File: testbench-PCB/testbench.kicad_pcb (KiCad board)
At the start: 2 copper layers, 185.4 x 134.6 mm, 68 parts, among them J1 USB_C_Receptacle_USB2.0, J2 AVR-ISP, J3 AVR-JTAG, SW1 SW_Push, U1 ATmega2561-16A, U10 CH340C, U2 Thermistor_module, U3 Rotary_encoder_switch_module, U4 RTC_EEPROM_module, U6 Relay_module, U7 Matrix_keyboard, U8 LCD_display, U9 USBLC6-2SC6, Y1 X322516MLB4SI

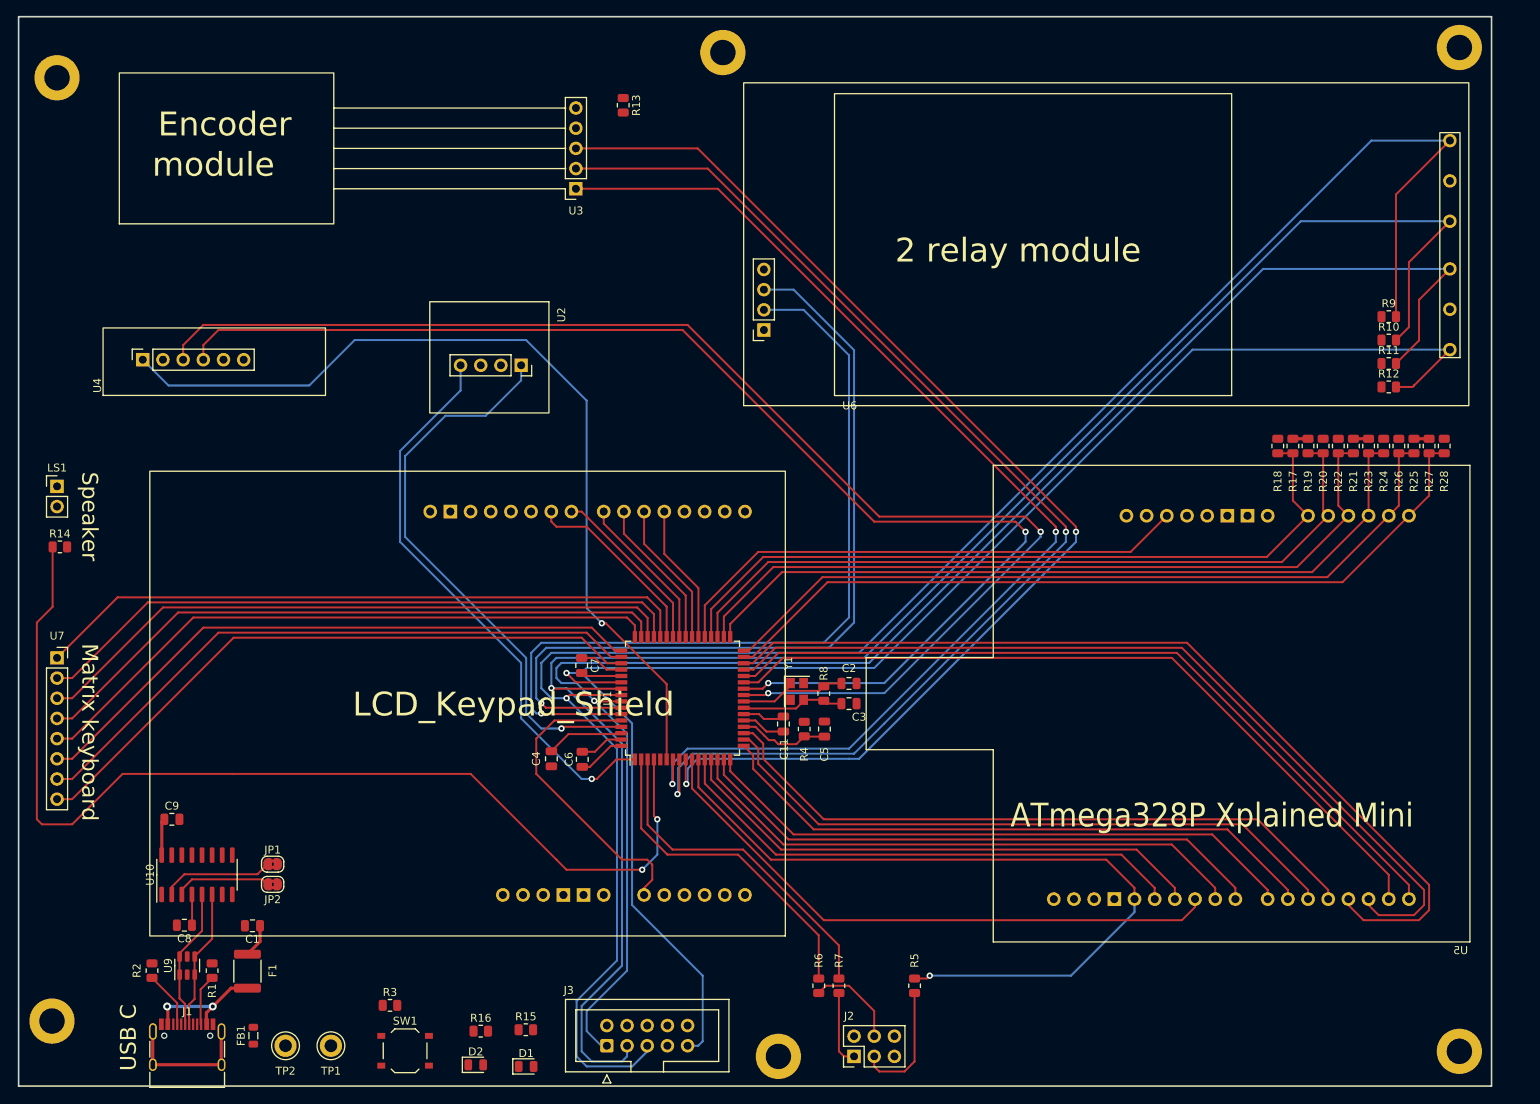
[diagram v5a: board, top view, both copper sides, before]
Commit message: Finished PCB routing, added ground plane.
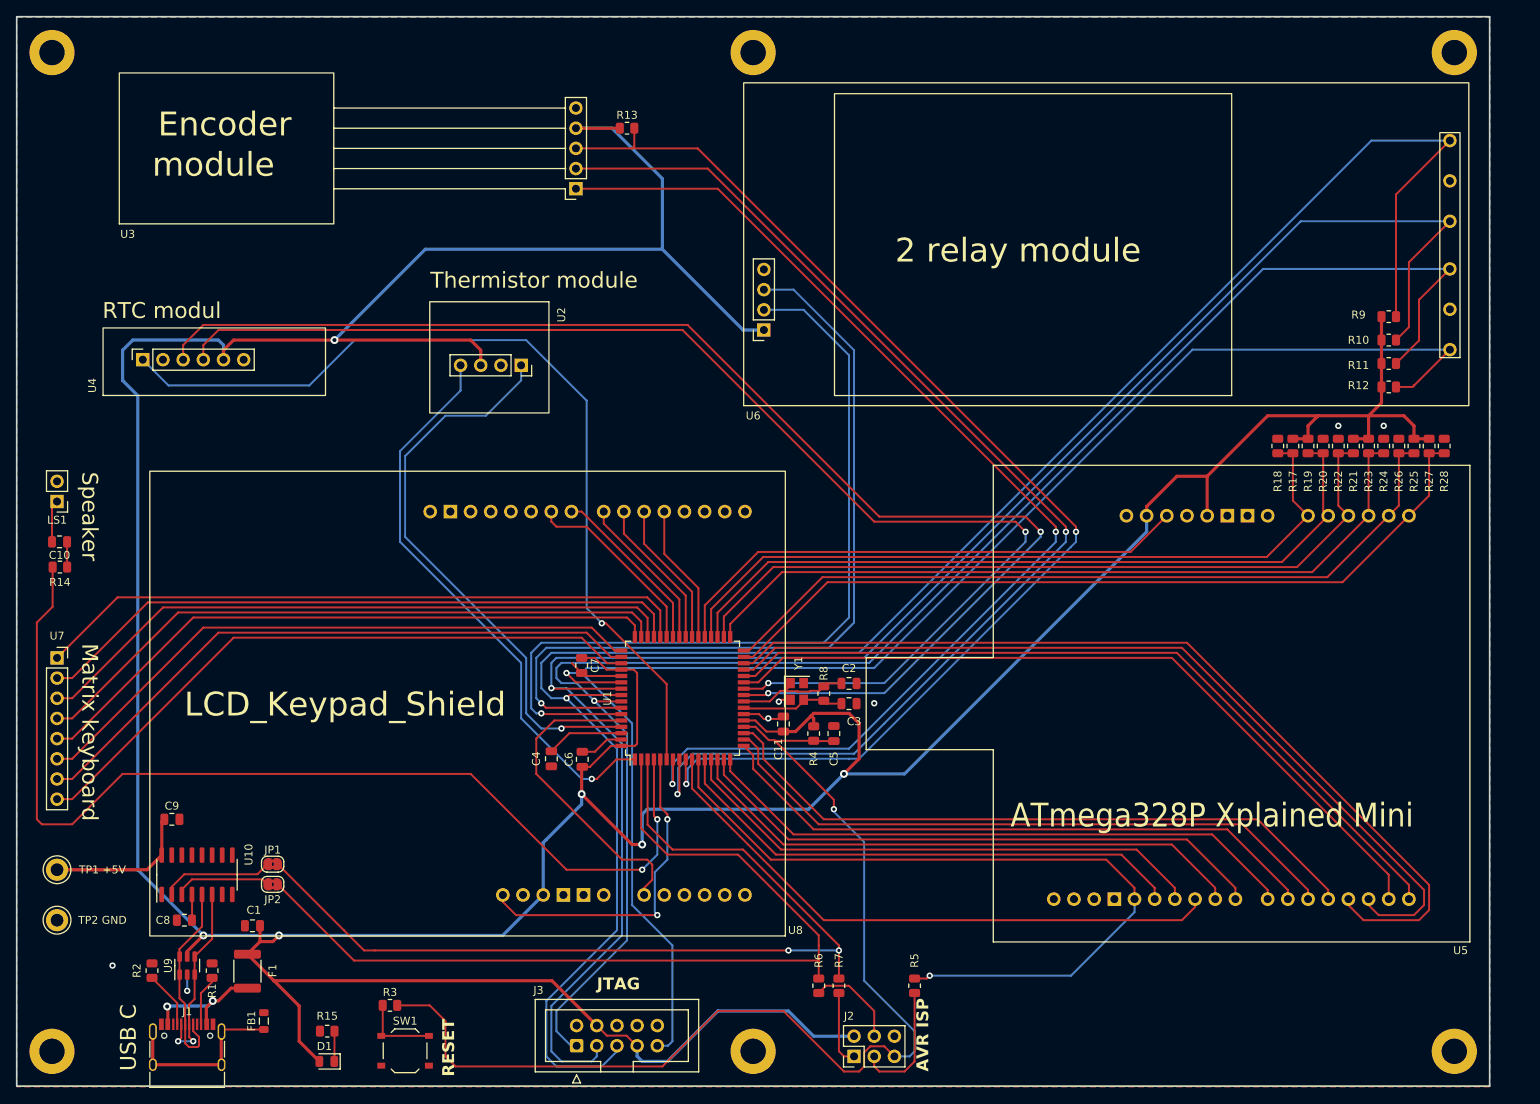
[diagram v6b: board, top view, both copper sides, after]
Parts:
- removed D2: LED, LED_SMD:LED_0805_2012Metric
- removed R16: 500R, Resistor_SMD:R_0805_2012Metric
- added C10: 1uF, Capacitor_SMD:C_0805_2012Metric, F.Cu at (43.5, 93.3)
- TP1 +5V: renamed from TP1
- TP2 GND: renamed from TP2
- moved TP1 +5V 41.0 mm to (43.2, 134.6)
- moved TP2 GND 32.8 mm to (43.2, 141.0)
- moved D1 25.1 mm to (77.1, 158.8), turned to 180 degrees
- moved R15 25.0 mm to (77.2, 154.9), turned to 180 degrees
- moved J3 3.81 mm to (108.6, 156.8)
- moved REF** 3.81 mm to (130.8, 31.8)
- moved REF** 3.81 mm to (42.5, 157.5)
- moved REF** 3.24 mm to (130.8, 157.5)
- moved REF** 3.24 mm to (42.5, 31.8)
- moved R13 2.93 mm to (114.9, 41.3), turned to 0 degrees
- moved R14 2.54 mm to (43.5, 96.5)
- moved FB1 2.27 mm to (69.2, 153.7)
- moved LS1 1.91 mm to (43.2, 88.3), turned to 180 degrees
- moved C5 1.32 mm to (141.0, 117.5)
- moved R4 1.32 mm to (138.4, 117.5)
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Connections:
- U1 pad 5: unconnected-(U1-PE3-Pad5) -> /Kit modules/LCD_D6
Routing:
- net +5V: track 31.8 -> 638.3 mm, vias 0 -> 6
- net /MCU/RST: track 11.5 -> 138.7 mm, vias 0 -> 1
- net /MCU/UART0_TXD: track 42.8 -> 117.9 mm, vias 0 -> 2
- net /MCU/UART0_RXD: track 42.0 -> 114.1 mm
- net /Kit modules/LCD_D6: track 0.00 -> 41.8 mm, vias 0 -> 2
- net Net-(R3-Pad1): track 0.00 -> 9.92 mm
- net Net-(U10-UD+): track 17.8 -> 25.2 mm
- net Net-(U10-UD-): track 17.6 -> 24.1 mm, vias 0 -> 2
- net GND: track 16.1 -> 21.7 mm, vias 0 -> 7
- net Net-(J1-SHIELD): track 17.0 -> 22.4 mm
- net Net-(C10-Pad2): track 0.00 -> 5.34 mm
- net Net-(D1-K): track 0.00 -> 3.82 mm
- net Net-(C10-Pad1): track 0.00 -> 3.18 mm
- net /Kit modules/ENC.SW: track 150.4 -> 153.1 mm
- net /Kit modules/Speaker_IN: track 134.1 -> 131.5 mm
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- added copper zone on B.Cu, net GND
- added copper zone on F.Cu, net GND
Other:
- board text added: "AVR ISP"
- board text added: "JTAG"
- board text added: "RESET"
- board text added: "RTC modul"
- board text added: "Thermistor module"

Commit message: Resolved DRC warnings and errors.
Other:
- board text added: "RTC module"
- board text removed: "RTC modul"

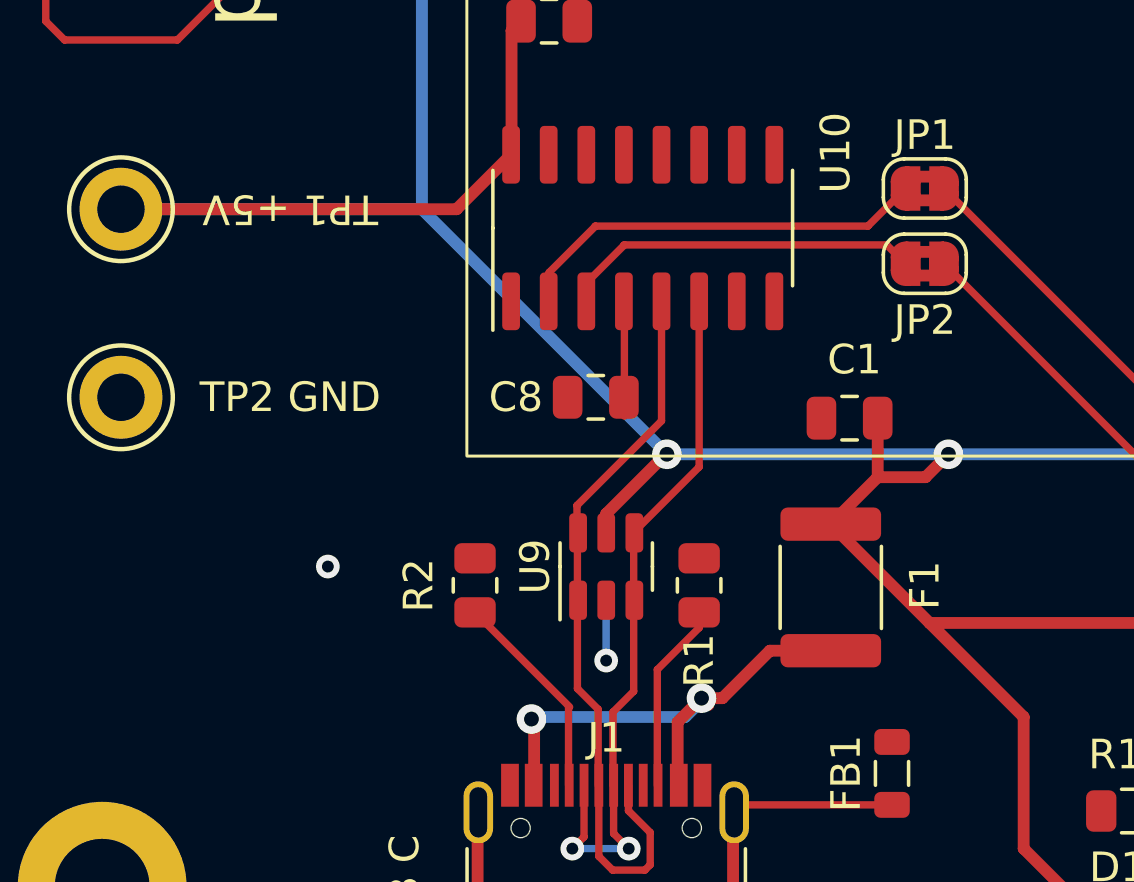
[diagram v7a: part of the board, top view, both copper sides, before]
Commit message: Changes regarding part selection.
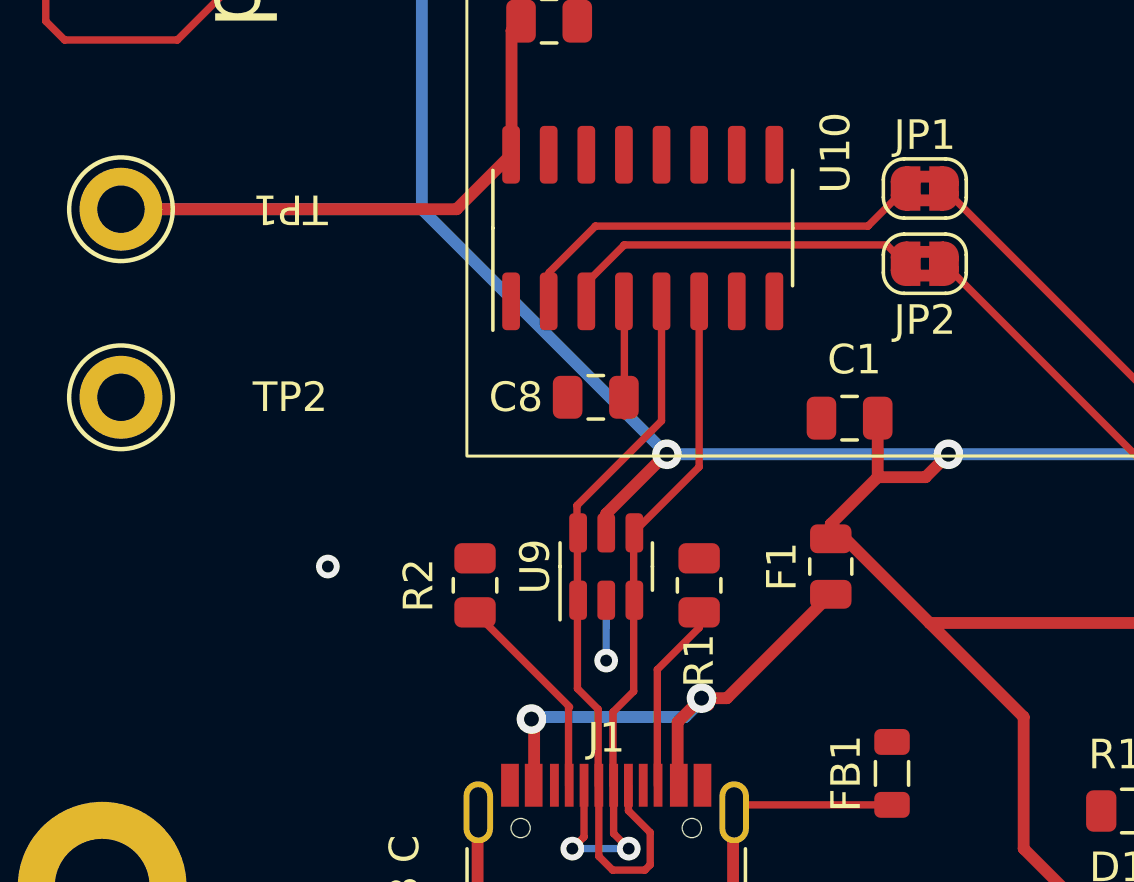
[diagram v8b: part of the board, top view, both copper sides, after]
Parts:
- C1: value 10u -> 4.7uF
- F1: value Polyfuse -> 500mA; footprint Fuse:Fuse_1812_4532Metric -> Fuse:Fuse_0805_2012Metric
- R15: value 500R -> 470R
- TP1: renamed from TP1 +5V
- TP2: renamed from TP2 GND
- moved F1 0.70 mm to (67.1, 146.7)
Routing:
- net /USB Interface/VBUS: track 17.0 -> 17.8 mm
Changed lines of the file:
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@@
     (property "ki_keywords" "test point tp")
     (attr through_hole)
-    (fp_text reference "TP2 GND" (at 5.715 0 unlocked) (layer "F.SilkS")
+    (fp_text reference "TP2" (at 5.715 0 unlocked) (layer "F.SilkS")
         (effects (font (size 1 1) (thickness 0.153)))
     )
@@
         (effects (font (size 1 1) (thickness 0.153)))
     )
-    (fp_text value "10u" (at 0 1.68 unlocked) (layer "F.Fab")
+    (fp_text value "4.7uF" (at 0 1.68 unlocked) (layer "F.Fab")
         (effects (font (size 1 1) (thickness 0.15)))
     )
@@
         (effects (font (size 1 1) (thickness 0.153)))
     )
-    (fp_text value "500R" (at 0 1.65 unlocked) (layer "F.Fab")
+    (fp_text value "470R" (at 0 1.65 unlocked) (layer "F.Fab")
         (effects (font (size 1 1) (thickness 0.15)))
     )
@@
     (property "ki_keywords" "test point tp")
     (attr through_hole)
-    (fp_text reference "TP1 +5V" (at 5.715 0 180 unlocked) (layer "F.SilkS")
+    (fp_text reference "TP1" (at 5.715 0 180 unlocked) (layer "F.SilkS")
         (effects (font (size 1 1) (thickness 0.153)))
     )
@@
     )
   )
-  (footprint "Fuse:Fuse_1812_4532Metric" (layer "F.Cu")
-    (at 67.1475 147.39 90)
-    (descr "Fuse SMD 1812 (4532 Metric), square (rectangular) end terminal, IPC_7351 nominal, (Body size source: https://www.nikhef.nl/pub/departments/mt/projects/detectorR_D/dtddice/ERJ2G.pdf), generated with kicad-footprint-generator")
+  (footprint "Fuse:Fuse_0805_2012Metric" (layer "F.Cu")
+    (at 67.1475 146.685 90)
+    (descr "Fuse SMD 0805 (2012 Metric), square (rectangular) end terminal, IPC_7351 nominal, (Body size source: https://docs.google.com/spreadsheets/d/1BsfQQcO9C6DZCsRaXUlFlo91Tg2WpOkGARC1WS5S8t0/edit?usp=sharing), generated with kicad-footprint-generator")
     (tags "fuse")
     (property "Sheetfile" "usb_interface.kicad_sch")
@@
     (property "ki_keywords" "resettable fuse PTC PPTC polyfuse polyswitch")
     (attr smd)
-    (fp_text reference "F1" (at 0.07 3.175 90 unlocked) (layer "F.SilkS")
+    (fp_text reference "F1" (at 0 -1.65 90) (layer "F.SilkS")
         (effects (font (size 1 1) (thickness 0.153)))
     )
-    (fp_text value "Polyfuse" (at 0 2.65 90 unlocked) (layer "F.Fab")
+    (fp_text value "500mA" (at 0 1.65 90) (layer "F.Fab")
         (effects (font (size 1 1) (thickness 0.15)))
     )
-    (fp_text user "${REFERENCE}" (at 0 0 90 unlocked) (layer "F.Fab")
-        (effects (font (size 1 1) (thickness 0.15)))
+    (fp_text user "${REFERENCE}" (at 0 0 90) (layer "F.Fab")
+        (effects (font (size 0.5 0.5) (thickness 0.08)))
     )
-    (fp_line (start -1.386252 -1.71) (end 1.386252 -1.71)
+    (fp_line (start -0.258578 -0.71) (end 0.258578 -0.71)
       (stroke (width 0.12) (type solid)) (layer "F.SilkS"))
-    (fp_line (start -1.386252 1.71) (end 1.386252 1.71)
+    (fp_line (start -0.258578 0.71) (end 0.258578 0.71)
       (stroke (width 0.12) (type solid)) (layer "F.SilkS"))
-    (fp_line (start -2.95 -1.95) (end 2.95 -1.95)
+    (fp_line (start -1.68 -0.95) (end 1.68 -0.95)
       (stroke (width 0.05) (type solid)) (layer "F.CrtYd"))
-    (fp_line (start -2.95 1.95) (end -2.95 -1.95)
+    (fp_line (start -1.68 0.95) (end -1.68 -0.95)
       (stroke (width 0.05) (type solid)) (layer "F.CrtYd"))
-    (fp_line (start 2.95 -1.95) (end 2.95 1.95)
+    (fp_line (start 1.68 -0.95) (end 1.68 0.95)
       (stroke (width 0.05) (type solid)) (layer "F.CrtYd"))
-    (fp_line (start 2.95 1.95) (end -2.95 1.95)
+    (fp_line (start 1.68 0.95) (end -1.68 0.95)
       (stroke (width 0.05) (type solid)) (layer "F.CrtYd"))
-    (fp_line (start -2.25 -1.6) (end 2.25 -1.6)
+    (fp_line (start -1 -0.6) (end 1 -0.6)
       (stroke (width 0.1) (type solid)) (layer "F.Fab"))
-    (fp_line (start -2.25 1.6) (end -2.25 -1.6)
+    (fp_line (start -1 0.6) (end -1 -0.6)
       (stroke (width 0.1) (type solid)) (layer "F.Fab"))
-    (fp_line (start 2.25 -1.6) (end 2.25 1.6)
+    (fp_line (start 1 -0.6) (end 1 0.6)
       (stroke (width 0.1) (type solid)) (layer "F.Fab"))
-    (fp_line (start 2.25 1.6) (end -2.25 1.6)
+    (fp_line (start 1 0.6) (end -1 0.6)
       (stroke (width 0.1) (type solid)) (layer "F.Fab"))
-    (pad "1" smd roundrect (at -2.1375 0 90) (size 1.125 3.4) (layers "F.Cu" "F.Paste" "F.Mask") (roundrect_rratio 0.222222)
+    (pad "1" smd roundrect (at -0.9375 0 90) (size 0.975 1.4) (layers "F.Cu" "F.Paste" "F.Mask") (roundrect_rratio 0.25)
       (net 80 "/USB Interface/VBUS") (pintype "passive"))
-    (pad "2" smd roundrect (at 2.1375 0 90) (size 1.125 3.4) (layers "F.Cu" "F.Paste" "F.Mask") (roundrect_rratio 0.222222)
+    (pad "2" smd roundrect (at 0.9375 0 90) (size 0.975 1.4) (layers "F.Cu" "F.Paste" "F.Mask") (roundrect_rratio 0.25)
       (net 3 "+5V") (pintype "passive"))
-    (model "${KICAD6_3DMODEL_DIR}/Fuse.3dshapes/Fuse_1812_4532Metric.wrl"
+    (model "${KICAD6_3DMODEL_DIR}/Fuse.3dshapes/Fuse_0805_2012Metric.wrl"
       (offset (xyz 0 0 0))
       (scale (xyz 1 1 1))
@@
   (segment (start 59.565 145.5475) (end 59.565 144.905) (width 0.4) (layer "F.Cu") (net 3))
   (segment (start 195.58 77.47) (end 201.93 77.47) (width 0.4) (layer "F.Cu") (net 3))
+  (segment (start 67.1475 145.7475) (end 67.1475 145.2525) (width 0.4) (layer "F.Cu") (net 3))
   (segment (start 208.28 77.47) (end 208.28 80.3675) (width 0.4) (layer "F.Cu") (net 3))
   (segment (start 64.135 69.215) (end 65.405 67.945) (width 0.4) (layer "F.Cu") (net 3))
@@
   (segment (start 62.7825 151.13) (end 61.9775 151.935) (width 0.4) (layer "F.Cu") (net 80))
   (segment (start 62.7825 151.13) (end 63.015 151.3625) (width 0.4) (layer "F.Cu") (net 80))
-  (segment (start 65.09 149.5275) (end 67.1475 149.5275) (width 0.4) (layer "F.Cu") (net 80))
+  (segment (start 63.64 151.13) (end 67.1475 147.6225) (width 0.4) (layer "F.Cu") (net 80))
   (segment (start 57.13 151.925) (end 57.13 154.07) (width 0.4) (layer "F.Cu") (net 80))
   (segment (start 57.04 151.835) (end 57.13 151.925) (width 0.4) (layer "F.Cu") (net 80))
-  (segment (start 62.7825 151.13) (end 63.4875 151.13) (width 0.4) (layer "F.Cu") (net 80))
-  (segment (start 63.4875 151.13) (end 65.09 149.5275) (width 0.4) (layer "F.Cu") (net 80))
+  (segment (start 62.7825 151.13) (end 63.64 151.13) (width 0.4) (layer "F.Cu") (net 80))
   (via (at 57.04 151.835) (size 1) (drill 0.5) (layers "F.Cu" "B.Cu") (net 80))
   (via (at 62.7825 151.13) (size 1) (drill 0.5) (layers "F.Cu" "B.Cu") (net 80))
